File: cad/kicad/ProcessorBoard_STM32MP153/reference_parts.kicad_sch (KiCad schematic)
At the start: 0 parts

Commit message: some more caps and power specs
maybe puppy and rainbows if dont use the sw controlled PMIC. ddr dosent seem to care too much about sequencing, and the mpu sequence is 2 steps... but size :( :( :( . wheres muh leaded puckagies :(
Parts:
- added C901: 22u, Capacitor_SMD:C_0603_1608Metric_Pad1.08x0.95mm_HandSolder, symbol Device:C_Small
- added C902: 10u, Capacitor_SMD:C_0603_1608Metric_Pad1.08x0.95mm_HandSolder, symbol Device:C_Small
- added C903: 1u, Capacitor_SMD:C_0603_1608Metric_Pad1.08x0.95mm_HandSolder, symbol Device:C_Small
- added L901: 1u, Inductor_SMD:L_1008_2520Metric_Pad1.43x2.20mm_HandSolder, symbol Device:L_Small
- added R901: 3090, Resistor_SMD:R_0603_1608Metric_Pad0.98x0.95mm_HandSolder, symbol Device:R_Small_US
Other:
- note added: "MLCC ~20V"
- note added: "MLCC ~5V"

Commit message: respeced caps
everything out of stok :(
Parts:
- added C904: 1u, Capacitor_SMD:C_01005_0402Metric_Pad0.57x0.30mm_HandSolder, symbol Device:C_Small
- C903: value 1u -> 4.7u; footprint Capacitor_SMD:C_0603_1608Metric_Pad1.08x0.95mm_HandSolder -> Capacitor_SMD:C_01005_0402Metric_Pad0.57x0.30mm_HandSolder; character https://ds.yuden.co.jp/TYCOMPAS/ap/detail?pn=MSASE168SB7105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 -> https://ds.murata.com/simsurfing/mlcc.html?partnumbers=%5B%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; mouser https://www.mouser.com/en/ProductDetail/Samsung-Electro-Mec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 -> https://www.mouser.com/en/ProductDetail/Murata-Electronics/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; unit x1 0.29 -> 0.047; unit x10 0.168 -> 0.11
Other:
- moved on the sheet: C901, C903
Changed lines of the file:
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@@
+	)
+	(symbol
+		(lib_id "Device:C_Small")
+		(at 80.01 90.17 0)
+		(unit 1)
+		(body_style 1)
+		(exclude_from_sim no)
+		(in_bom yes)
+		(on_board yes)
+		(in_pos_files yes)
+		(dnp no)
+		(fields_autoplaced yes)
+		(property "Reference" "C904"
+			(at 82.55 88.9062 0)
+			(show_name no)
+			(do_not_autoplace no)
+			(effects
+				(font
+					(size 1.27 1.27)
+				)
+				(justify left)
+			)
+		)
+		(property "Value" "1u"
+			(at 82.55 91.4462 0)
+			(show_name no)
+			(do_not_autoplace no)
+			(effects
+				(font
+					(size 1.27 1.27)
+				)
+				(justify left)
+			)
+		)
+		(property "Footprint" "Capacitor_SMD:C_01005_0402Metric_Pad0.57x0.30mm_HandSolder"
+			(at 80.01 90.17 0)
+			(hide yes)
+			(show_name no)
+			(do_not_autoplace no)
+			(effects
+				(font
+					(size 1.27 1.27)
+				)
+			)
+		)
+		(property "Datasheet" ""
+			(at 80.01 90.17 0)
+			(hide yes)
+			(show_name no)
+			(do_not_autoplace no)
+			(effects
+				(font
+					(size 1.27 1.27)
+				)
+			)
+		)
+		(property "Description" "1uF, 50Vdc, 10%, 10MHz"
+			(at 80.01 90.17 0)
+			(hide yes)
+			(show_name no)
+			(do_not_autoplace no)
+			(effects
+				(font
+					(size 1.27 1.27)
+				)
+			)
+		)
+		(property "mouser" "https://www.mouser.com/en/ProductDetail/Murata-Electronics/GRM155R61H105KE05J?qs=d0WKAl%252BL4KZilUxqJ3m7lA%3D%3D"
+			(at 80.01 90.17 0)
+			(hide yes)
+			(show_name no)
+			(do_not_autoplace no)
+			(effects
+				(font
+					(size 1.27 1.27)
+				)
+			)
+		)
+		(property "unit x10" "0.04"
+			(at 80.01 90.17 0)
+			(hide yes)
+			(show_name no)
+			(do_not_autoplace no)
+			(effects
+				(font
+					(size 1.27 1.27)
+				)
+			)
+		)
+		(property "unit x1" "0.11"
+			(at 80.01 90.17 0)
+			(hide yes)
+			(show_name no)
+			(do_not_autoplace no)
+			(effects
+				(font
+					(size 1.27 1.27)
+				)
+			)
+		)
+		(property "character" "https://ds.murata.com/simsurfing/mlcc.html?partnumbers=%5B%22GRM155R61H105KE05%22%5D&oripartnumbers=%5B%22GRM155R61H105KE05J%22%5D&rgear=suaykx&rgearinfo=com"
+			(at 80.01 90.17 0)
+			(hide yes)
+			(show_name no)
+			(do_not_autoplace no)
+			(effects
+				(font
+					(size 1.27 1.27)
+				)
+			)
+		)
+		(pin "1"
+		)
+		(pin "2"
+		)
+		(instances
+			(project "ProcessorBoard_STM32MP153"
+				(path "/e63e39d7-6ac0-4ffd-8aa3-1841a4541b55/157228c5-c462-4e2c-89a8-acc0a1fe94b2"
+					(reference "C904")
+					(unit 1)
+				)
+			)
+		)
 	)
 	(symbol
@@
 	(symbol
 		(lib_id "Device:C_Small")
-		(at 80.01 90.17 0)
+		(at 31.75 88.9 0)
 		(unit 1)
 		(body_style 1)
@@
 		(fields_autoplaced yes)
 		(property "Reference" "C903"
-			(at 82.55 88.9062 0)
-			(show_name no)
-			(do_not_autoplace no)
-			(effects
-				(font
-					(size 1.27 1.27)
-				)
-				(justify left)
-			)
-		)
-		(property "Value" "1u"
-			(at 82.55 91.4462 0)
-			(show_name no)
-			(do_not_autoplace no)
-			(effects
-				(font
-					(size 1.27 1.27)
-				)
-				(justify left)
-			)
-		)
-		(property "Footprint" "Capacitor_SMD:C_0603_1608Metric_Pad1.08x0.95mm_HandSolder"
-			(at 80.01 90.17 0)
+			(at 34.29 87.6362 0)
+			(show_name no)
+			(do_not_autoplace no)
+			(effects
+				(font
+					(size 1.27 1.27)
+				)
+				(justify left)
+			)
+		)
+		(property "Value" "4.7u"
+			(at 34.29 90.1762 0)
+			(show_name no)
+			(do_not_autoplace no)
+			(effects
+				(font
+					(size 1.27 1.27)
+				)
+				(justify left)
+			)
+		)
+		(property "Footprint" "Capacitor_SMD:C_01005_0402Metric_Pad0.57x0.30mm_HandSolder"
+			(at 31.75 88.9 0)
 			(hide yes)
 			(show_name no)
@@
 		)
 		(property "Datasheet" ""
-			(at 80.01 90.17 0)
-			(hide yes)
-			(show_name no)
-			(do_not_autoplace no)
-			(effects
-				(font
-					(size 1.27 1.27)
-				)
-			)
-		)
-		(property "Description" "1uF, 16V, 10%, 8.6MHz"
-			(at 80.01 90.17 0)
-			(hide yes)
-			(show_name no)
-			(do_not_autoplace no)
-			(effects
-				(font
-					(size 1.27 1.27)
-				)
-			)
-		)
-		(property "mouser" "https://www.mouser.com/en/ProductDetail/Samsung-Electro-Mechanics/CL10A106MA8NRWC?qs=ST9lo4GX8V1EuSEdq9MnFw%3D%3D"
-			(at 80.01 90.17 0)
-			(hide yes)
-			(show_name no)
-			(do_not_autoplace no)
-			(effects
-				(font
-					(size 1.27 1.27)
-				)
-			)
-		)
-		(property "unit x10" "0.168"
-			(at 80.01 90.17 0)
-			(hide yes)
-			(show_name no)
-			(do_not_autoplace no)
-			(effects
-				(font
-					(size 1.27 1.27)
-				)
-			)
-		)
-		(property "unit x1" "0.29"
-			(at 80.01 90.17 0)
-			(hide yes)
-			(show_name no)
-			(do_not_autoplace no)
-			(effects
-				(font
-					(size 1.27 1.27)
-				)
-			)
-		)
-		(property "character" "https://ds.yuden.co.jp/TYCOMPAS/ap/detail?pn=MSASE168SB7105KTNA01&u=M"
-			(at 80.01 90.17 0)
+			(at 31.75 88.9 0)
+			(hide yes)
+			(show_name no)
+			(do_not_autoplace no)
+			(effects
+				(font
+					(size 1.27 1.27)
+				)
+			)
+		)
+		(property "Description" "4.7uF, 6.3Vdc, 20%, 4MHz"
+			(at 31.75 88.9 0)
+			(hide yes)
+			(show_name no)
+			(do_not_autoplace no)
+			(effects
+				(font
+					(size 1.27 1.27)
+				)
+			)
+		)
+		(property "mouser" "https://www.mouser.com/en/ProductDetail/Murata-Electronics/GRM155R60J475ME47J?qs=hNud%2FORuBR1o1%2F4Jg%2F%2FSnQ%3D%3D&srsltid=AU7gw4Xa6q2PLsvpnK6qcDhvS62mgMLyQXdMzXB2DHlvS5Pd_XhfAXxY"
+			(at 31.75 88.9 0)
+			(hide yes)
+			(show_name no)
+			(do_not_autoplace no)
+			(effects
+				(font
+					(size 1.27 1.27)
+				)
+			)
+		)
+		(property "unit x10" "0.11"
+			(at 31.75 88.9 0)
+			(hide yes)
+			(show_name no)
+			(do_not_autoplace no)
+			(effects
+				(font
+					(size 1.27 1.27)
+				)
+			)
+		)
+		(property "unit x1" "0.047"
+			(at 31.75 88.9 0)
+			(hide yes)
+			(show_name no)
+			(do_not_autoplace no)
+			(effects
+				(font
+					(size 1.27 1.27)
+				)
+			)
+		)
+		(property "character" "https://ds.murata.com/simsurfing/mlcc.html?partnumbers=%5B%22GRM155R60J475ME47%22%5D&oripartnumbers=%5B%22GRM155R60J475ME47J%22%5D&rgear=suaykx&rgearinfo=com"
+			(at 31.75 88.9 0)
 			(hide yes)
 			(show_name no)
@@
 	(symbol
 		(lib_id "Device:C_Small")
-		(at 22.86 91.44 0)
+		(at 19.05 88.9 0)
 		(unit 1)
 		(body_style 1)
@@
 		(fields_autoplaced yes)
 		(property "Reference" "C901"
-			(at 25.4 90.1762 0)
+			(at 21.59 87.6362 0)
 			(show_name no)
 			(do_not_autoplace no)
@@
 		)
 		(property "Value" "22u"
-			(at 25.4 92.7162 0)
+			(at 21.59 90.1762 0)
 			(show_name no)
 			(do_not_autoplace no)
@@
 		)
 		(property "Footprint" "Capacitor_SMD:C_0603_1608Metric_Pad1.08x0.95mm_HandSolder"
-			(at 22.86 91.44 0)
+			(at 19.05 88.9 0)
 			(hide yes)
 			(show_name no)
@@
 		)
 		(property "Datasheet" ""
-			(at 22.86 91.44 0)
+			(at 19.05 88.9 0)
 			(hide yes)
 			(show_name no)
@@
 		)
 		(property "Description" "6.3VDC, 20%, medical, +85C, 1.8MHz"
-			(at 22.86 91.44 0)
+			(at 19.05 88.9 0)
 			(hide yes)
 			(show_name no)
@@
 		)
 		(property "mouser" "https://www.mouser.com/en/ProductDetail/TAIYO-YUDEN/MLASJ168BB5226MTNA01?qs=sGAEpiMZZMsh%252B1woXyUXj3XUfju0vRpjetlJTHUhUyk%3D"
-			(at 22.86 91.44 0)
+			(at 19.05 88.9 0)
 			(hide yes)
 			(show_name no)
@@
 		)
 		(property "unit x10" "0.112"
-			(at 22.86 91.44 0)
+			(at 19.05 88.9 0)
 			(hide yes)
 			(show_name no)
@@
 		)
 		(property "character" "https://ds.yuden.co.jp/TYCOMPAS/ut/detail?pn=MLASJ168BB5226MTNA01&u=M"
-			(at 22.86 91.44 0)
+			(at 19.05 88.9 0)
 			(hide yes)
 			(show_name no)
@@
 		)
 		(property "unit x1" "0.27"
-			(at 22.86 91.44 0)
-			(hide yes)
-			(show_name no)
+			(at 19.05 88.9 0)
+			(hide yes)
+			(show_name no)

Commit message: mpu power connections
about mpu, apparently onboard usb supply has a requirement for the onboard ldo's to be happy, so u have to tap out 2 deticated pins. and theres also a power off sequence as well???
1v8 life looking better every day, 3v3(>2v9) trenches over there
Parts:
- added C905: 1n, Capacitor_SMD:C_01005_0402Metric_Pad0.57x0.30mm_HandSolder, symbol Device:C_Small
- added C906: 100n, Capacitor_SMD:C_01005_0402Metric_Pad0.57x0.30mm_HandSolder, symbol Device:C_Small
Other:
- note added: "small bga stuff ~0402"

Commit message: mr przudent get down
a thrid DDR voltage requirement has hit the power plane.
the cost of 11$ ram is apparently 3 distinct power nets :( .
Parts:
- added R902: 47k, Resistor_SMD:R_0603_1608Metric_Pad0.98x0.95mm_HandSolder, symbol Device:R_Small_US
- added R903: 1.2k, Resistor_SMD:R_0603_1608Metric_Pad0.98x0.95mm_HandSolder, symbol Device:R_Small_US
- added R904: 240, Capacitor_SMD:C_0402_1005Metric_Pad0.74x0.62mm_HandSolder, symbol Device:R_Small_US
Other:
- note removed: "small bga stuff ~0402"
- moved on the sheet: C905, C906, R901

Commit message: is this tuff
most datasheets from LCSC are "not for public release"
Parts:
- added R905: 10k, Capacitor_SMD:C_0402_1005Metric_Pad0.74x0.62mm_HandSolder, symbol Device:R_Small_US
- added R906: 1k, Capacitor_SMD:C_0402_1005Metric_Pad0.74x0.62mm_HandSolder, symbol Device:R_Small_US
- added R907: 10, Resistor_SMD:R_0402_1005Metric_Pad0.72x0.64mm_HandSolder, symbol Device:R_Small_US
- C906: footprint Capacitor_SMD:C_01005_0402Metric_Pad0.57x0.30mm_HandSolder -> Capacitor_SMD:C_0402_1005Metric_Pad0.74x0.62mm_HandSolder
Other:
- moved on the sheet: R901, R903

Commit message: big ol kicad file ?
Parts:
- removed R902: 47k, Resistor_SMD:R_0603_1608Metric_Pad0.98x0.95mm_HandSolder, symbol Device:R_Small_US
- added L99901: 2.2u, Inductor_SMD:L_Ferrocore_DLG-0302, symbol Device:L_Small
- added R99901: 45.3k, Resistor_SMD:R_0603_1608Metric_Pad0.98x0.95mm_HandSolder, symbol Device:R_Small_US
- R905: footprint Capacitor_SMD:C_0402_1005Metric_Pad0.74x0.62mm_HandSolder -> Resistor_SMD:R_0603_1608Metric_Pad0.98x0.95mm_HandSolder; mouser https://www.mouser.com/en/ProductDetail/YAGEO/RT0402FRE0710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 -> https://www.mouser.com/en/ProductDetail/SEI-Stackpole/RNCF0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; unit x10 0.013 -> 0.071; unit x100 0.012 -> 0.067
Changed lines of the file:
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@@
 	(symbol
 		(lib_id "Device:R_Small_US")
-		(at 20.32 20.32 0)
+		(at 19.05 20.32 0)
 		(unit 1)
 		(body_style 1)
@@
 		(dnp no)
 		(fields_autoplaced yes)
-		(property "Reference" "R902"
-			(at 22.86 19.0499 0)
-			(show_name no)
-			(do_not_autoplace no)
-			(effects
-				(font
-					(size 1.27 1.27)
-				)
-				(justify left)
-			)
-		)
-		(property "Value" "47k"
-			(at 22.86 21.5899 0)
+		(property "Reference" "R99901"
+			(at 21.59 19.0499 0)
+			(show_name no)
+			(do_not_autoplace no)
+			(effects
+				(font
+					(size 1.27 1.27)
+				)
+				(justify left)
+			)
+		)
+		(property "Value" "45.3k"
+			(at 21.59 21.5899 0)
 			(show_name no)
 			(do_not_autoplace no)
@@
 		)
 		(property "Footprint" "Resistor_SMD:R_0603_1608Metric_Pad0.98x0.95mm_HandSolder"
-			(at 20.32 20.32 0)
+			(at 19.05 20.32 0)
 			(hide yes)
 			(show_name no)
@@
 		)
 		(property "Datasheet" ""
-			(at 20.32 20.32 0)
-			(hide yes)
-			(show_name no)
-			(do_not_autoplace no)
-			(effects
-				(font
-					(size 1.27 1.27)
-				)
-			)
-		)
-		(property "Description" "47kR, 150V, 1%, 0.2W, 100ppm, +155C"
-			(at 20.32 20.32 0)
-			(hide yes)
-			(show_name no)
-			(do_not_autoplace no)
-			(effects
-				(font
-					(size 1.27 1.27)
-				)
-			)
-		)
-		(property "mouser" "https://www.mouser.com/en/ProductDetail/KOA-Speer/SG73P1JTTD4702F?qs=sGAEpiMZZMvdGkrng054t%2Fj9PfXFS6zMQ9Jwo5NzY3U%3D"
-			(at 20.32 20.32 0)
-			(hide yes)
-			(show_name no)
-			(do_not_autoplace no)
-			(effects
-				(font
-					(size 1.27 1.27)
-				)
-			)
-		)
-		(property "unit x1" "0.12"
-			(at 20.32 20.32 0)
-			(hide yes)
-			(show_name no)
-			(do_not_autoplace no)
-			(effects
-				(font
-					(size 1.27 1.27)
-				)
-			)
-		)
-		(property "unit x10" "0.37"
-			(at 20.32 20.32 0)
-			(hide yes)
-			(show_name no)
-			(do_not_autoplace no)
-			(effects
-				(font
-					(size 1.27 1.27)
-				)
-			)
-		)
-		(property "unit x100" "0.31"
-			(at 20.32 20.32 0)
+			(at 19.05 20.32 0)
+			(hide yes)
+			(show_name no)
+			(do_not_autoplace no)
+			(effects
+				(font
+					(size 1.27 1.27)
+				)
+			)
+		)
+		(property "Description" "45.3kR, 0.1%, 100mW, 25ppm, 75V, +155C"
+			(at 19.05 20.32 0)
+			(hide yes)
+			(show_name no)
+			(do_not_autoplace no)
+			(effects
+				(font
+					(size 1.27 1.27)
+				)
+			)
+		)
+		(property "mouser" "https://www.mouser.com/en/ProductDetail/YAGEO/RT0603BRD0745K3L?qs=sGAEpiMZZMvdGkrng054t98Xz4DA4UW4K0WmzVPNprg%3D"
+			(at 19.05 20.32 0)
+			(hide yes)
+			(show_name no)
+			(do_not_autoplace no)
+			(effects
+				(font
+					(size 1.27 1.27)
+				)
+			)
+		)
+		(property "unit x1" "0.10"
+			(at 19.05 20.32 0)
+			(hide yes)
+			(show_name no)
+			(do_not_autoplace no)
+			(effects
+				(font
+					(size 1.27 1.27)
+				)
+			)
+		)
+		(property "unit x10" "0.06"
+			(at 19.05 20.32 0)
+			(hide yes)
+			(show_name no)
+			(do_not_autoplace no)
+			(effects
+				(font
+					(size 1.27 1.27)
+				)
+			)
+		)
+		(property "unit x100" "0.056"
+			(at 19.05 20.32 0)
 			(hide yes)
 			(show_name no)
@@
 			(project "ProcessorBoard_STM32MP153"
 				(path "/e63e39d7-6ac0-4ffd-8aa3-1841a4541b55/157228c5-c462-4e2c-89a8-acc0a1fe94b2"
-					(reference "R902")
+					(reference "R99901")
 					(unit 1)
 				)
@@
 	)
 	(symbol
+		(lib_id "Device:L_Small")
+		(at 27.94 148.59 0)
+		(unit 1)
+		(body_style 1)
+		(exclude_from_sim no)
+		(in_bom yes)
+		(on_board yes)
+		(in_pos_files yes)
+		(dnp no)
+		(fields_autoplaced yes)
+		(property "Reference" "L99901"
+			(at 29.21 147.3199 0)
+			(show_name no)
+			(do_not_autoplace no)
+			(effects
+				(font
+					(size 1.27 1.27)
+				)
+				(justify left)
+			)
+		)
+		(property "Value" "2.2u"
+			(at 29.21 149.8599 0)
+			(show_name no)
+			(do_not_autoplace no)
+			(effects
+				(font
+					(size 1.27 1.27)
+				)
+				(justify left)
+			)
+		)
+		(property "Footprint" "Inductor_SMD:L_Ferrocore_DLG-0302"
+			(at 27.94 148.59 0)
+			(hide yes)
+			(show_name no)
+			(do_not_autoplace no)
+			(effects
+				(font
+					(size 1.27 1.27)
+				)
+			)
+		)
+		(property "Datasheet" ""
+			(at 27.94 148.59 0)
+			(hide yes)
+			(show_name no)
+			(do_not_autoplace no)
+			(effects
+				(font
+					(size 1.27 1.27)
+				)
+			)
+		)
+		(property "Description" "2.2uH, %20, 29MHz, 60mR, 3A"
+			(at 27.94 148.59 0)
+			(hide yes)
+			(show_name no)
+			(do_not_autoplace no)
+			(effects
+				(font
+					(size 1.27 1.27)
+				)
+			)
+		)
+		(property "mouser" "https://www.mouser.com/en/ProductDetail/ABRACON/AOTA-N252010S-2R2MT?qs=4dK74SdgGtzQq9i9FaXoWg%3D%3D"
+			(at 27.94 148.59 0)
+			(hide yes)
+			(show_name no)
+			(do_not_autoplace no)
+			(effects
+				(font
+					(size 1.27 1.27)
+				)
+			)
+		)
+		(property "unit x1" "0.22"
+			(at 27.94 148.59 0)
+			(hide yes)
+			(show_name no)
+			(do_not_autoplace no)
+			(effects
+				(font
+					(size 1.27 1.27)
+				)
+			)
+		)
+		(property "unit x10" "0.182"
+			(at 27.94 148.59 0)
+			(hide yes)
+			(show_name no)
+			(do_not_autoplace no)
+			(effects
+				(font
+					(size 1.27 1.27)
+				)
+			)
+		)
+		(pin "2"
+		)
+		(pin "1"
+		)
+		(instances
+			(project "ProcessorBoard_STM32MP153"
+				(path "/e63e39d7-6ac0-4ffd-8aa3-1841a4541b55/157228c5-c462-4e2c-89a8-acc0a1fe94b2"
+					(reference "L99901")
+					(unit 1)
+				)
+			)
+		)
+	)
+	(symbol
 		(lib_id "Device:R_Small_US")
 		(at 31.75 20.32 0)
@@
 			)
 		)
-		(property "Footprint" "Capacitor_SMD:C_0402_1005Metric_Pad0.74x0.62mm_HandSolder"
+		(property "Footprint" "Resistor_SMD:R_0603_1608Metric_Pad0.98x0.95mm_HandSolder"
 			(at 31.75 20.32 0)
 			(hide yes)
@@
 			)
 		)
-		(property "Description" "10kR, 63.5mW, 50Vdc, 1%, 50ppm, +155c"
+		(property "Description" "10kR, 100mW, 75Vdc, 0.1%, 25ppm, +155c"
 			(at 31.75 20.32 0)
 			(hide yes)
@@
 			)
 		)
-		(property "mouser" "https://www.mouser.com/en/ProductDetail/YAGEO/RT0402FRE0710KL?qs=sGAEpiMZZMvdGkrng054t8AJgcdMkx7xfPhHYA%2FCigo%3D"
+		(property "mouser" "https://www.mouser.com/en/ProductDetail/SEI-Stackpole/RNCF0603BTE10K0?qs=sGAEpiMZZMvdGkrng054t2cqbZCzJY7NKyrLU8aYXDErcCrjgif2eA%3D%3D"
 			(at 31.75 20.32 0)
 			(hide yes)
@@
 			)
 		)
-		(property "unit x10" "0.013"
+		(property "unit x10" "0.071"
 			(at 31.75 20.32 0)
 			(hide yes)
@@
 			)
 		)
-		(property "unit x100" "0.012"
+		(property "unit x100" "0.067"
 			(at 31.75 20.32 0)
 			(hide yes)

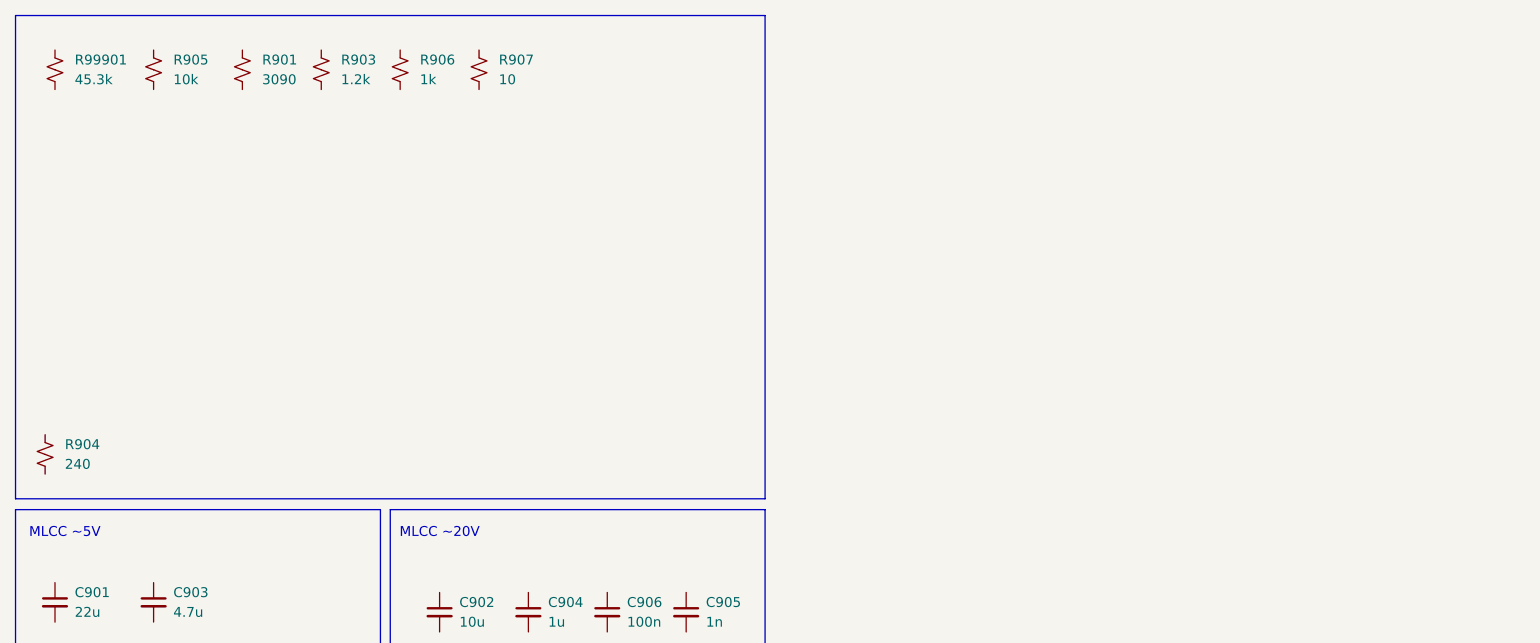
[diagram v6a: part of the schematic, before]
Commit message: new ram
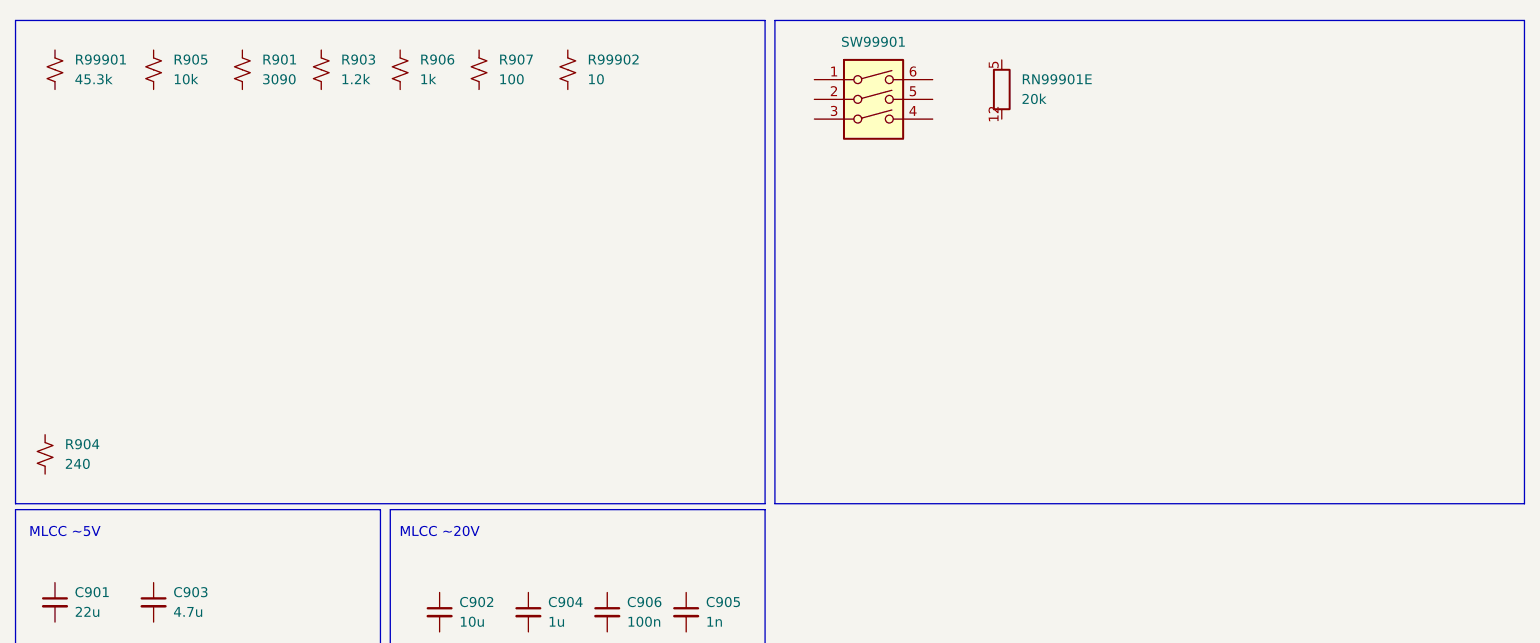
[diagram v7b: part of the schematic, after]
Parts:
- added R99902: 10, Resistor_SMD:R_0402_1005Metric_Pad0.72x0.64mm_HandSolder, symbol Device:R_Small_US
- added RN99901: 20k, zzLocalLibraries-Footprints:R_array_EXB2HV_8, symbol Device:R_Pack08_Split
- added SW99901: SW_DIP_x03, Button_Switch_SMD:SW_DIP_SPSTx03_Slide_Omron_A6S-310x_W8.9mm_P2.54mm, symbol Switch:SW_DIP_x03
- R907: value 10 -> 100; mouser https://www.mouser.com/en/ProductDetail/Bourns/CR0402-FX-10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 -> https://www.mouser.com/en/ProductDetail/KOA-Speer/RN73R1ETT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; unit x1 0.1 -> 0.10; unit x10 0.009 -> 0.061; unit x100 0.007 -> (none)
